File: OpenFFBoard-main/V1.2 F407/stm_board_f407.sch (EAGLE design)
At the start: 60 parts, among them J1 10118193-0001LF, SW1 TL3342F160QG/TR, SW2 TL3342F160QG/TR, U1 STM32F407VGT6, U2 TJA1051T/3, U3 LM1117, X1 8MHz

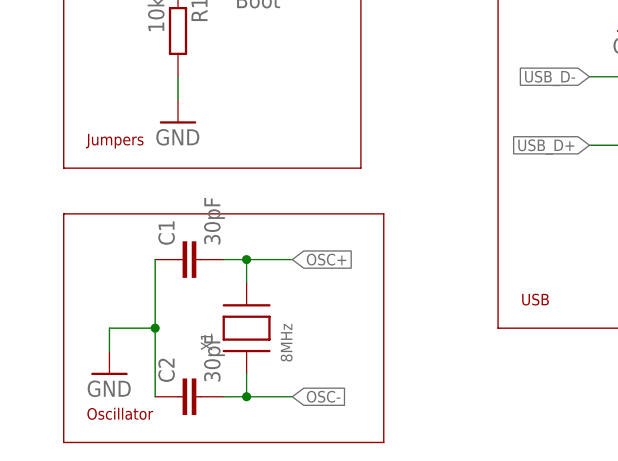
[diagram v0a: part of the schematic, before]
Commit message: Updated crystal capacitor value
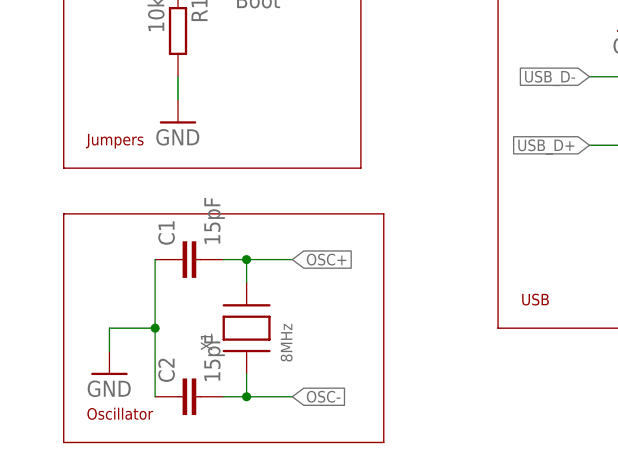
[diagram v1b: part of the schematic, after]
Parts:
- C1, C2: value 30pF -> 15pF
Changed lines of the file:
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@@
 <?xml version="1.0" encoding="utf-8"?>
 <!DOCTYPE eagle SYSTEM "eagle.dtd">
-<eagle version="9.3.1">
+<eagle version="9.6.2">
 <drawing>
 <settings>
@@
 <parts>
 <part name="FRAME1" library="frames" library_urn="urn:adsk.eagle:library:229" deviceset="A3L-LOC" device=""/>
-<part name="C1" library="resistor" library_urn="urn:adsk.eagle:library:348" deviceset="C-EU" device="C0603" package3d_urn="urn:adsk.eagle:package:23616/2" value="30pF"/>
-<part name="C2" library="resistor" library_urn="urn:adsk.eagle:library:348" deviceset="C-EU" device="C0603" package3d_urn="urn:adsk.eagle:package:23616/2" value="30pF"/>
+<part name="C1" library="resistor" library_urn="urn:adsk.eagle:library:348" deviceset="C-EU" device="C0603" package3d_urn="urn:adsk.eagle:package:23616/2" value="15pF"/>
+<part name="C2" library="resistor" library_urn="urn:adsk.eagle:library:348" deviceset="C-EU" device="C0603" package3d_urn="urn:adsk.eagle:package:23616/2" value="15pF"/>
 <part name="GND2" library="supply1" library_urn="urn:adsk.eagle:library:371" deviceset="GND" device=""/>
 <part name="J1" library="con_ampusb_10118193-0001LF" deviceset="10118193-0001LF" device=""/>

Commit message: Schematic for f407 updated
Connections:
- net ENC_Z: now also U1A.PD15; no longer U1A.PC8
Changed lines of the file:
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@@
 </segment>
 <segment>
-<wire x1="119.38" y1="215.9" x2="121.92" y2="215.9" width="0.1524" layer="91"/>
-<label x="121.92" y="215.9" size="1.27" layer="95" rot="MR180" xref="yes"/>
-<pinref part="U1" gate="A" pin="PC8"/>
+<wire x1="119.38" y1="154.94" x2="121.92" y2="154.94" width="0.1524" layer="91"/>
+<label x="121.92" y="154.94" size="1.27" layer="95" rot="MR180" xref="yes"/>
+<pinref part="U1" gate="A" pin="PD15"/>
 </segment>
 </net>
